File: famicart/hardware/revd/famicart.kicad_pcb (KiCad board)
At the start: 4 copper layers, 90 x 46.1 mm, 140 parts, among them J1 Famicom 60-pin edge, J2 RUN/GND, J3 USB-C PRG/mapper (U1) (HRO TY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, J4 USB-C CHR (U2) (HRO TYPE-C-31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, J5 SWD A (SWCLK GND SWDIO), J6 SWD B (SWCLK GND SWDIO), SW1 RESET, SW2 BOOTSEL A, SW3 BOOTSEL B, U1 RP2350B, U10 74LVC541 U10, U11 74LVC541 U11, U12 74LVC245 CPU data (console<->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, U13 74LVC1G11 AND3: CPU data enab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, U14 74LVC1G32 OR: CPU 245 /OE, U15 74LVC1G04 INV: R/W, U16 74LVC1G00 NAND: WRAM /WE, U17 74LVC541 U17, U18 74LVC541 U18, U19 74LVC245 PPU data (console<->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, U2 RP2350B, U20 74LVC00 PPU access / CIRAM gl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, U21 74LVC1G32 OR: PPU 245 /OE, U22 74LVC139 CHR ROM/RAM select, U24 74LVC245 CPU->PPU data bridge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, U26 74LVC1G07 OD: /IRQ A, U27 74LVC1G07 OD: /IRQ B, U28 AMS1117-3.3, U3 W25Q16JVSSIQ, U4 W25Q16JVSSIQ, U5 S29GL01GS 1Gbit NOR (x8 use), U6 S29GL01GS 1Gbit NOR (x8 use), U7 FM28V100 128Kx8 F-RAM (WRAM/s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, U8 IS62WV5128 512Kx8 SRAM, U9 74LVC541 U9, Y1 12MHz ABM8-272-T3, Y2 12MHz ABM8-272-T3

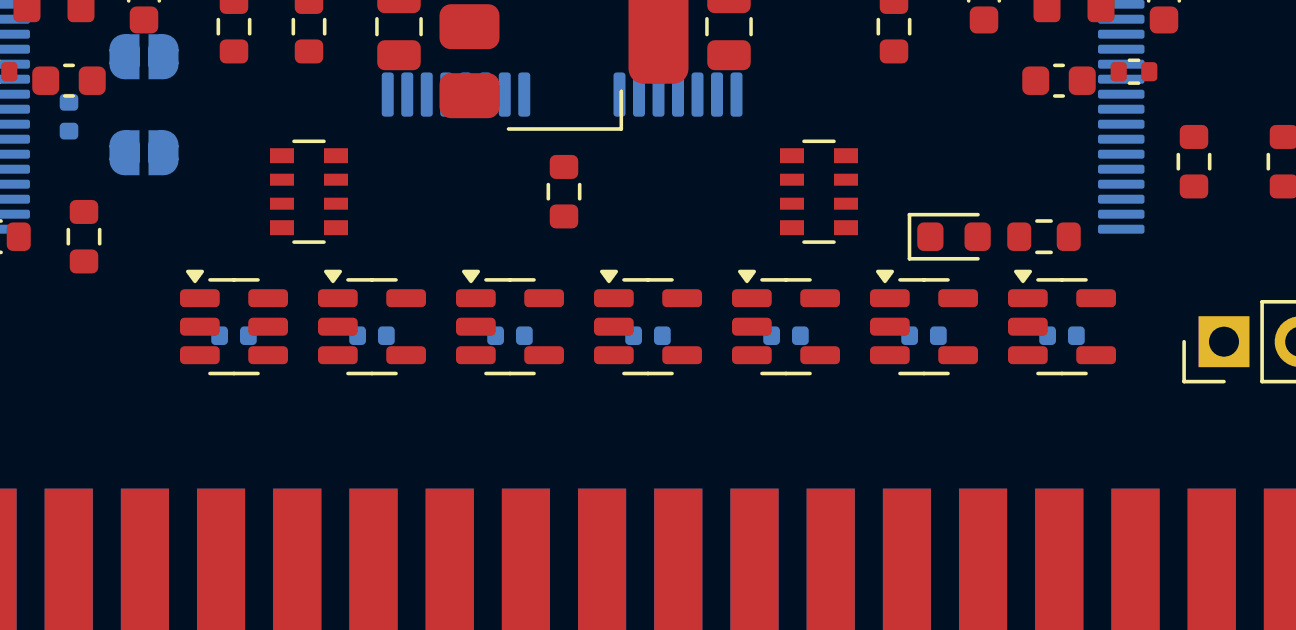
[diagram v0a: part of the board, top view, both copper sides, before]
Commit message: famicart/hardware rev D: board snapshot before routing (0.1 mm rules, gate row moved)
Co-Authored-By: Claude Fable 5.1 <noreply@anthropic.com>
Claude-Session: https://claude.ai/code/session_01RfF2rUHDV6Gz9CaznXPSPp
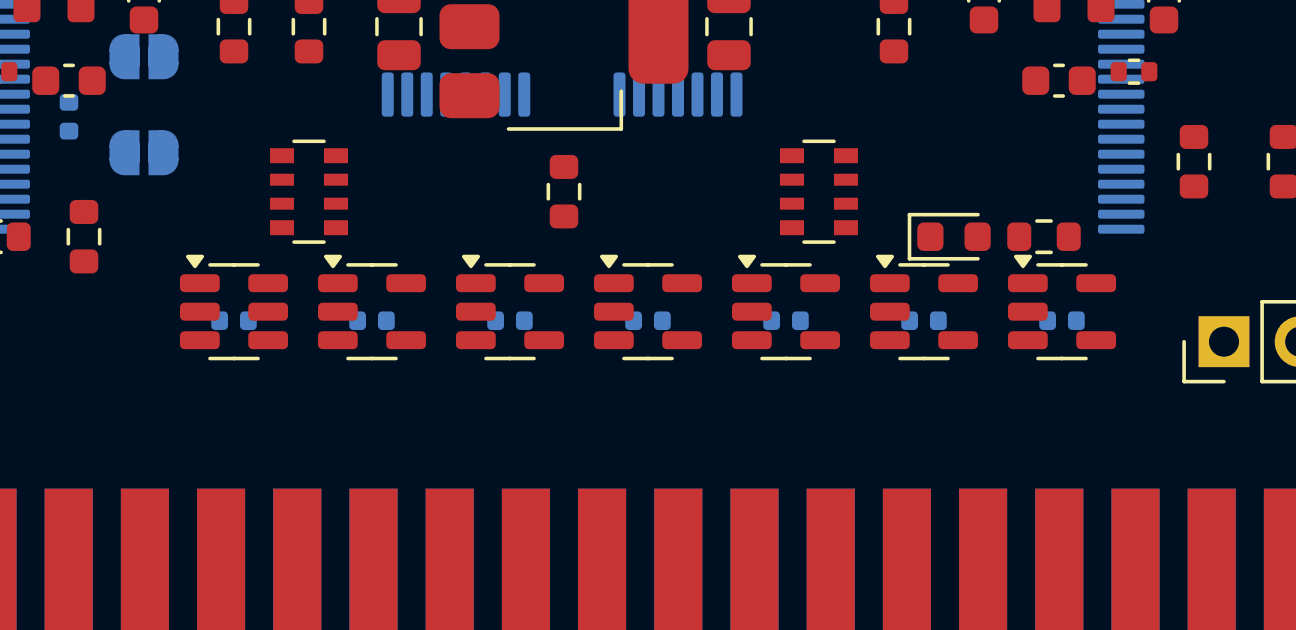
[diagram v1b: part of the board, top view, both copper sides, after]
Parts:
- moved C53 0.50 mm to (34.0, 32.8)
- moved C54 0.50 mm to (38.6, 32.8)
- moved C55 0.50 mm to (43.2, 32.8)
- moved C56 0.50 mm to (47.8, 32.8)
- moved C57 0.50 mm to (52.4, 32.8)
- moved C58 0.50 mm to (57.0, 32.8)
- moved C59 0.50 mm to (61.6, 32.8)
- moved U13 0.50 mm to (34.0, 32.5)
- moved U14 0.50 mm to (38.6, 32.5)
- moved U15 0.50 mm to (43.2, 32.5)
- moved U16 0.50 mm to (47.8, 32.5)
- moved U21 0.50 mm to (52.4, 32.5)
- moved U26 0.50 mm to (57.0, 32.5)
- moved U27 0.50 mm to (61.6, 32.5)

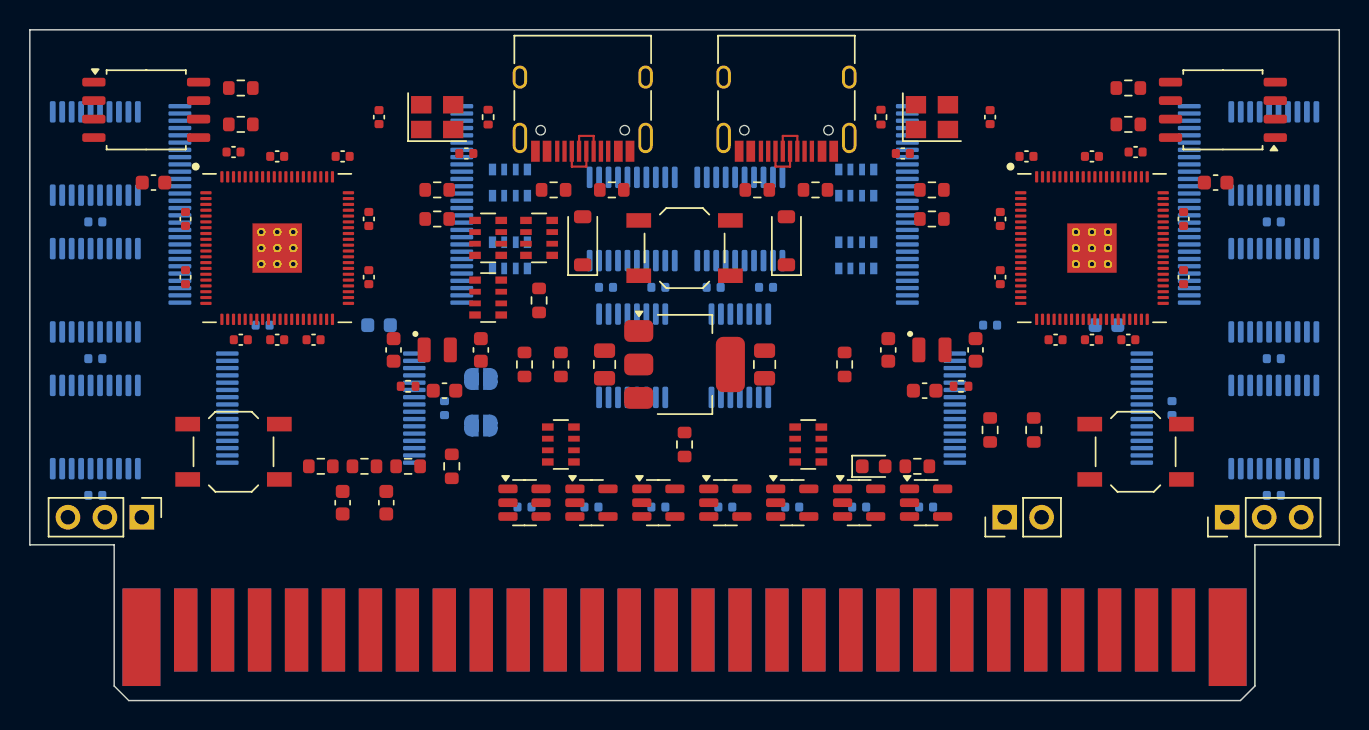
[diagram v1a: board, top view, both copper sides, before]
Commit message: famicart rev D: routed 6-layer board (0 unconnected, 0 DRC errors), gerbers, BOM, JLCPCB package
- Freerouting 1.9 (6 layers, ~30 min) -> 6 open connections, finished by finish_route.py
  (negotiated rip-up, plane vias) in 3 rounds; connectivity-safe cleanup of dangling stubs
  and duplicate vias. 6185 tracks, 609 vias; VREG_LX 1.9 mm, QSPI SCLK ~6 mm.
- hardware/revd: schematic, board, project with the board's design rules, 6-layer gerbers +
  drill, front/back/In2/In3 renders, bom.csv, jlcpcb/ (BOM with LCSC parts incl. S29GL01GS,
  FM28V100, IS62WV5128, USB-C; CPL; gerbers.zip; ordering notes for the 6-layer stack).
- gen_sch keeps a pcbnew-written project file and writes the FC_* rules; gen_jlc part keys fixed.
- docs: rev D routing result and the MCU placement rules.

Co-Authored-By: Claude Opus 5.5 <noreply@anthropic.com>
Claude-Session: https://claude.ai/code/session_01RfF2rUHDV6Gz9CaznXPSPp
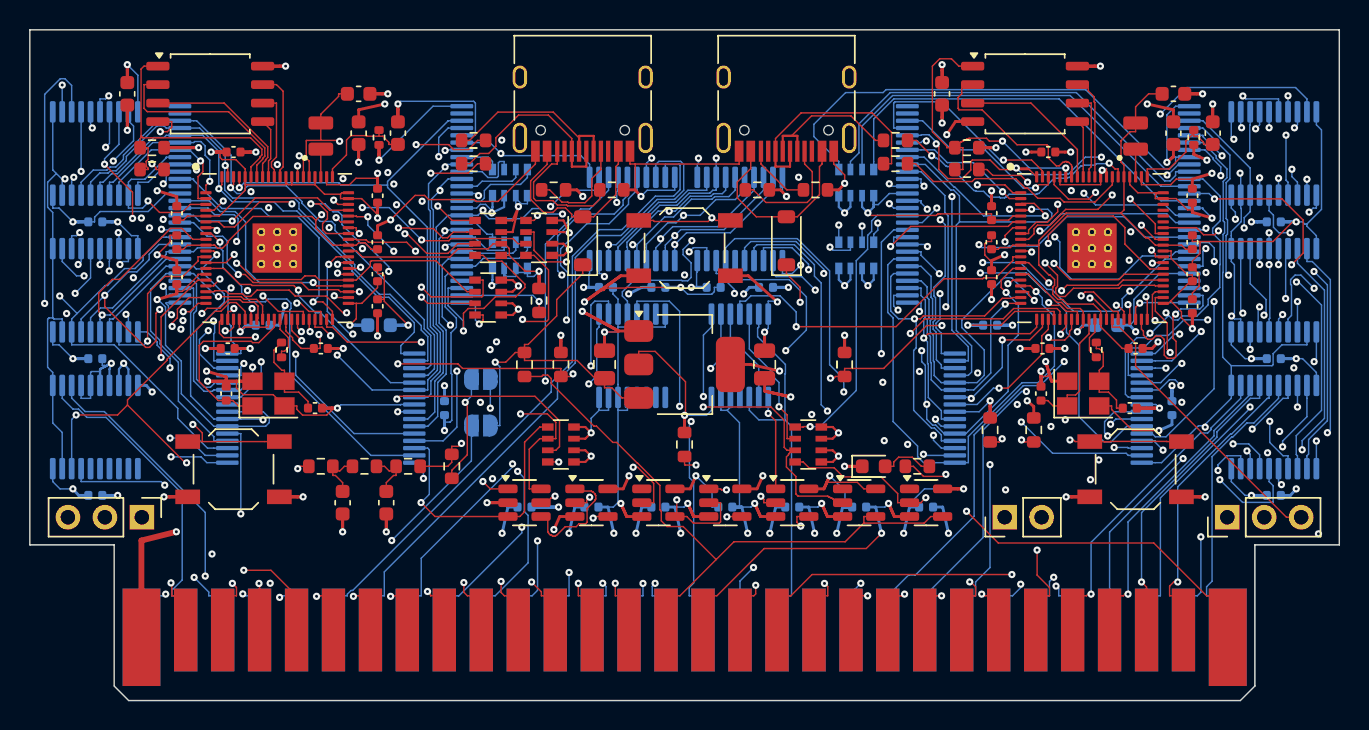
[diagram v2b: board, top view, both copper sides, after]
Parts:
- moved C22 26.6 mm to (81.3, 7.10), turned to 90 degrees
- moved C20 26.3 mm to (78.6, 4.40), turned to 0 degrees
- moved C19 23.4 mm to (75.6, 26.0)
- moved R10 23.4 mm to (80.0, 7.40), turned to 90 degrees
- moved Y1 22.3 mm to (16.4, 25.0)
- moved R9 21.8 mm to (73.3, 22.0)
- moved C2 21.7 mm to (13.5, 25.0)
- moved Y2 21.7 mm to (72.4, 25.0)
- moved R3 21.4 mm to (17.3, 22.0)
- moved C3 20.4 mm to (19.6, 26.0)
- moved L2 20.3 mm to (76.0, 7.30), turned to 90 degrees
- moved C21 20.2 mm to (78.6, 7.10)
- moved C17 19.8 mm to (62.7, 4.40), turned to 90 degrees
- moved C4 19.5 mm to (22.6, 4.40), turned to 0 degrees
- moved C18 19.3 mm to (69.5, 25.0)
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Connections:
- C20 pad 1: +3V3 -> +1V1B
- C21 pad 1: +1V1B -> +3V3
- C4 pad 1: +3V3 -> +1V1A
- C5 pad 1: +1V1A -> +3V3
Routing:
- net GND: track 0.00 -> 709.3 mm, vias 0 -> 79
- net +3V3: track 0.00 -> 657.0 mm, vias 0 -> 71
- net ISOLATE: track 0.00 -> 159.8 mm, vias 0 -> 10
- net RUN: track 0.00 -> 144.7 mm, vias 0 -> 7
- net PnRD: track 0.00 -> 115.7 mm, vias 0 -> 4
- net +5V: track 0.00 -> 90.3 mm, vias 0 -> 3
- net PD1: track 0.00 -> 87.2 mm, vias 0 -> 5
- net PD0: track 0.00 -> 81.1 mm, vias 0 -> 6
- net PD3: track 0.00 -> 80.8 mm, vias 0 -> 7
- net PD2: track 0.00 -> 80.1 mm, vias 0 -> 4
- net PD5: track 0.00 -> 79.3 mm, vias 0 -> 5
- net PD4: track 0.00 -> 78.5 mm, vias 0 -> 5
- net CnROMSEL: track 0.00 -> 77.2 mm, vias 0 -> 5
- net CD4: track 0.00 -> 77.1 mm, vias 0 -> 4
- net CD1: track 0.00 -> 76.8 mm, vias 0 -> 4
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- added copper zone on In4.Cu, net +3V3
- removed copper zone on In2.Cu, net +3V3
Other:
- copper layers 4 -> 6
